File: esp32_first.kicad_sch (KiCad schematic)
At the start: 28 parts, among them J10 Conn_01x02_Socket, J11 USB_C_Receptacle_USB2.0_16P, J12 Conn_01x03_Socket, J13 Conn_01x02_Socket, J14 Conn_01x02_Socket, SW3 SW_Wuerth_450301014042, U1 ESP32-WROOM-32E, U2 MCP2561-E-SN, U3 CH340E, U4 BD33FC0FP

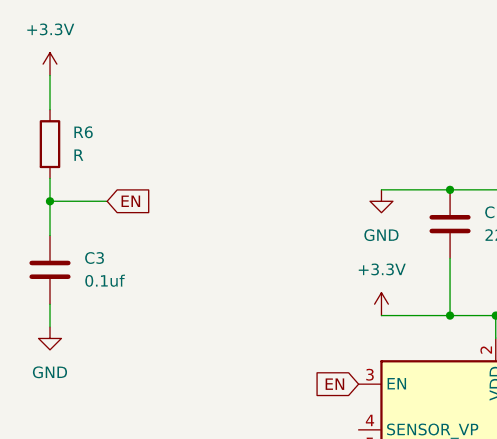
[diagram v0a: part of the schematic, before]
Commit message: STM基板から同じ部品のコピー、一部調整
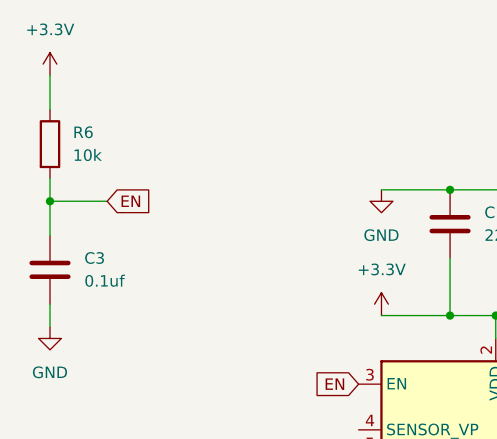
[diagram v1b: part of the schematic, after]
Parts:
- R6: value R -> 10k
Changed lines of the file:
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@@
 			)
 		)
-		(property "Value" "R"
+		(property "Value" "10k"
 			(at 31.75 27.9399 0)
 			(effects

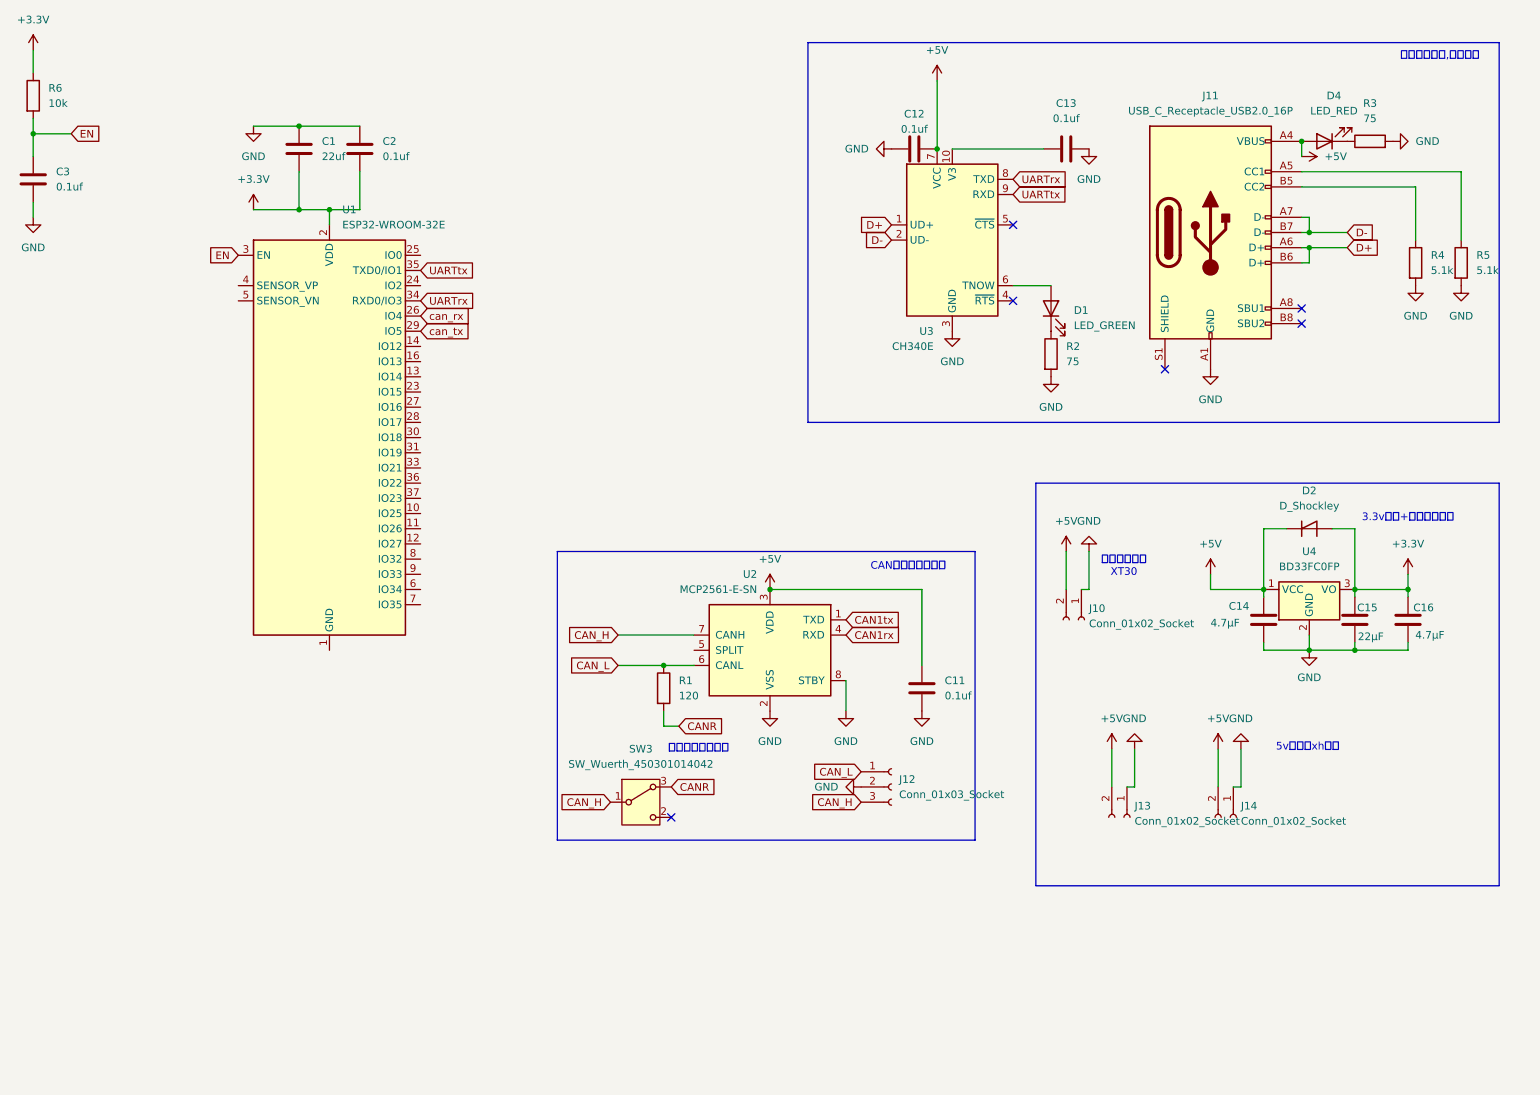
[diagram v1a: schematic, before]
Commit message: 書き込み回路の作成、不要な部品の削除
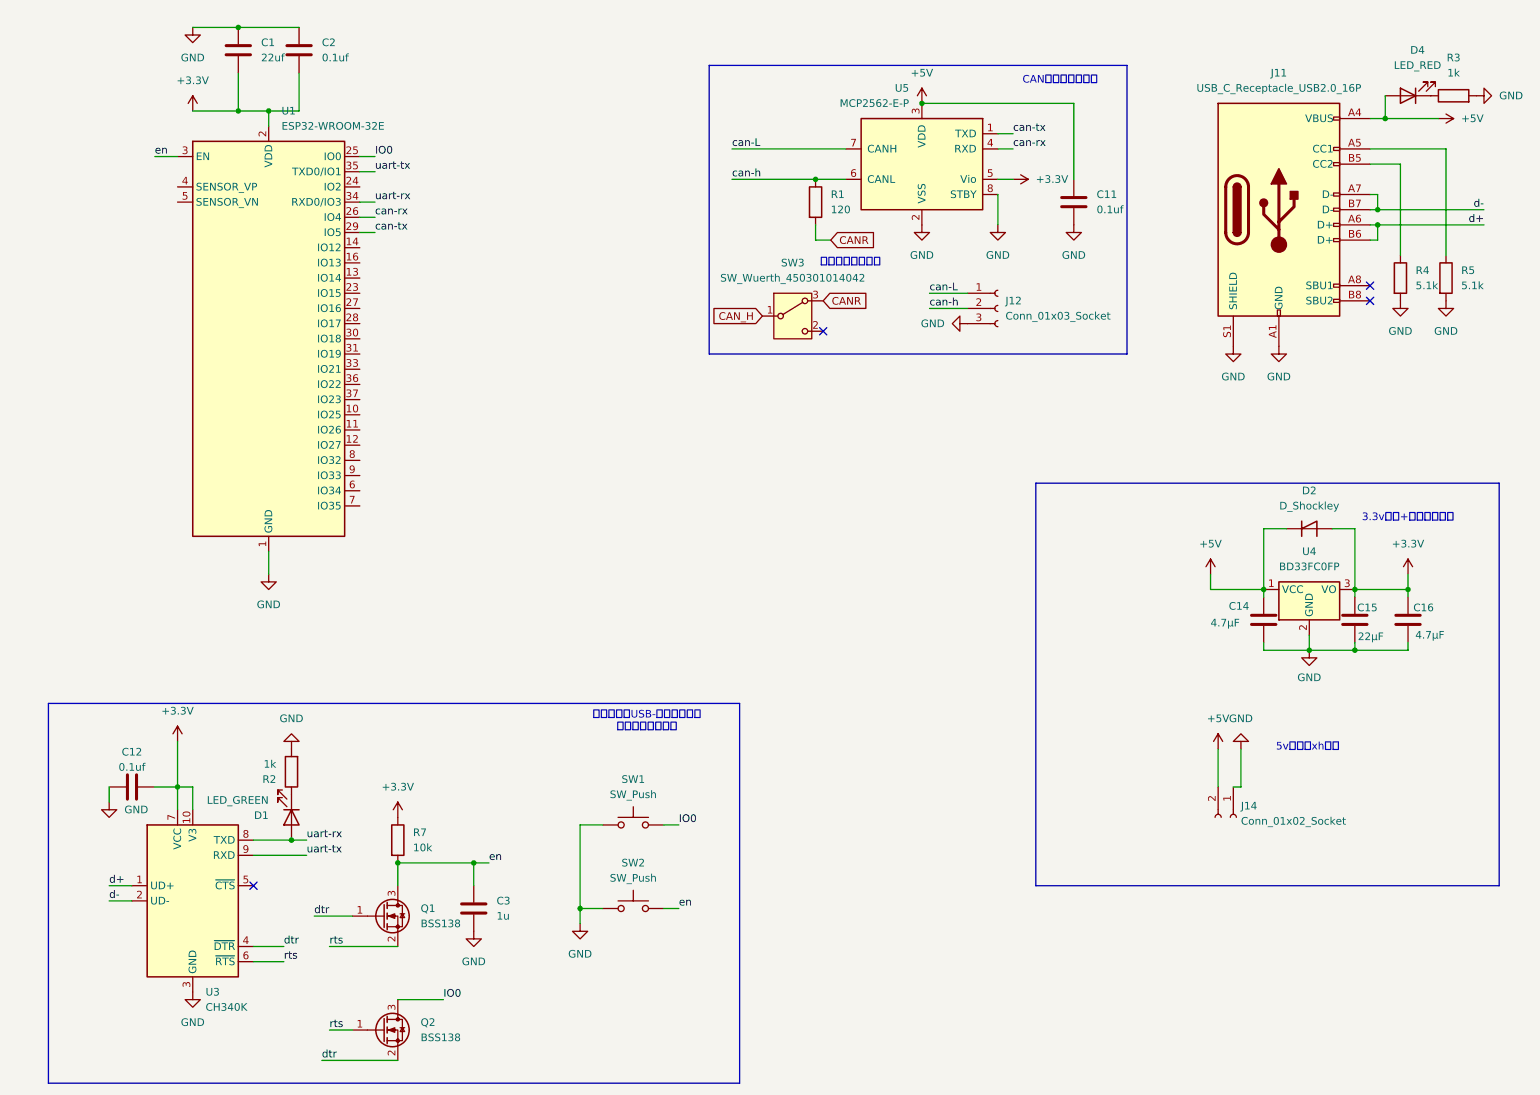
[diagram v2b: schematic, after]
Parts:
- removed C13: 0.1uf, Capacitor_SMD:C_0603_1608Metric_Pad1.08x0.95mm_HandSolder, symbol Device:C
- removed J10: Conn_01x02_Socket, Connector_AMASS:AMASS_XT30PW-F_1x02_P2.50mm_Horizontal, symbol Connector:Conn_01x02_Socket
- removed J13: Conn_01x02_Socket, Connector_JST:JST_XH_S2B-XH-A-1_1x02_P2.50mm_Horizontal, symbol Connector:Conn_01x02_Socket
- removed R6: 10k, symbol Device:R
- removed U2: MCP2561-E-SN, Package_SO:SOIC-8_3.9x4.9mm_P1.27mm, symbol Interface_CAN_LIN:MCP2561-E-SN
- removed U3: CH340E, Package_SO:MSOP-10_3x3mm_P0.5mm, symbol Interface_USB:CH340E
- added Q1, Q2: BSS138, Package_TO_SOT_SMD:SOT-23, symbol Transistor_FET:BSS138
- added R7: 10k, symbol Device:R
- added SW1, SW2: SW_Push, symbol Switch:SW_Push
- added U3: CH340K, Package_SO:SSOP-10-1EP_3.9x4.9mm_P1mm_EP2.1x3.3mm, symbol Interface_USB:CH340K
- added U5: MCP2562-E-P, Package_DIP:DIP-8_W7.62mm, symbol Interface_CAN_LIN:MCP2562-E-P
- C3: value 0.1uf -> 1u
- R2, R3: value 75 -> 1k
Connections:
- net UARTrx is gone; now on net uart-rx: U1.34 (RXD0/IO3)
- net +3.3V: now also C12.2, R7.1, U3.10 (V3), U3.7 (VCC), U5.5 (Vio)
- net +5V: now also U5.3 (VDD); no longer C12.2
- net CAN_H: no longer J12.3 (Pin_3)
- net GND: now also J11.S1 (SHIELD), J12.3 (Pin_3), U1.1 (GND), U1.15 (GND), U1.38 (GND), U1.39 (GND), SW1.1, SW2.1, U3.11 (GND), U3.3 (GND), U5.2 (VSS), U5.8 (STBY); no longer J12.2 (Pin_2)
- net IO0: now reaches U1.25 (IO0)
- net IO0: now also Q2.3 (D), SW1.2
- net uart-rx: now reaches D1.2 (A)
- net uart-rx: now also U3.8 (TXD)
- net CAN_L renamed can-L
- net can-L: now also U5.7 (CANH); no longer R1.1
- net D+ renamed d+
- net d+: now also U3.1 (UD+)
- net D- renamed d-
- net d-: now also U3.2 (UD-)
- net EN renamed en
- net en: now also Q1.3 (D), R7.2, SW2.2
- net UARTtx renamed uart-tx
- net uart-tx: now also U3.9 (RXD)
- net can_rx renamed can-rx
- net can-rx: now also U5.4 (RXD)
- net can_tx renamed can-tx
- net can-tx: now also U5.1 (TXD)
- new net can-h: J12.2 (Pin_2), R1.1, U5.6 (CANL)
- new net dtr: Q1.1 (G), Q2.2 (S), U3.4 (~{DTR})
- new net rts: Q1.2 (S), Q2.1 (G), U3.6 (~{RTS})
- no-connect marks 6 -> 4
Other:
- note added: "書き込み用USB-シリアル変換 書き込み認識回路"
- note removed: "シリアル通信,書き込み"
- note removed: "電源コネクタ XT30"
- moved on the sheet: C1, C11, C12, C2, D1, D4, J11, J12, R1, R2, R3, R4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

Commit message: フットプリントの割り当て
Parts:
- C1: footprint (none) -> Capacitor_SMD:C_0805_2012Metric_Pad1.18x1.45mm_HandSolder
- C2, C3: footprint (none) -> Capacitor_SMD:C_0603_1608Metric_Pad1.08x0.95mm_HandSolder
- R4, R5: footprint Resistor_SMD:R_1206_3216Metric_Pad1.30x1.75mm_HandSolder -> Resistor_SMD:R_0805_2012Metric_Pad1.20x1.40mm_HandSolder
- R7: footprint (none) -> Resistor_SMD:R_0805_2012Metric_Pad1.20x1.40mm_HandSolder
- SW1, SW2: footprint (none) -> Button_Switch_THT:SW_PUSH_6mm
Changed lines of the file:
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@@
 			)
 		)
-		(property "Footprint" ""
+		(property "Footprint" "Button_Switch_THT:SW_PUSH_6mm"
 			(at 129.54 143.51 0)
 			(effects
@@
 			)
 		)
-		(property "Footprint" ""
+		(property "Footprint" "Capacitor_SMD:C_0805_2012Metric_Pad1.18x1.45mm_HandSolder"
 			(at 64.4652 22.86 0)
 			(effects
@@
 			)
 		)
-		(property "Footprint" ""
+		(property "Footprint" "Capacitor_SMD:C_0603_1608Metric_Pad1.08x0.95mm_HandSolder"
 			(at 103.8352 166.37 0)
 			(effects
@@
 			)
 		)
-		(property "Footprint" "Resistor_SMD:R_1206_3216Metric_Pad1.30x1.75mm_HandSolder"
+		(property "Footprint" "Resistor_SMD:R_0805_2012Metric_Pad1.20x1.40mm_HandSolder"
 			(at 263.652 57.15 90)
 			(effects
@@
 			)
 		)
-		(property "Footprint" ""
+		(property "Footprint" "Capacitor_SMD:C_0603_1608Metric_Pad1.08x0.95mm_HandSolder"
 			(at 74.6252 22.86 0)
 			(effects
@@
 			)
 		)
-		(property "Footprint" ""
+		(property "Footprint" "Resistor_SMD:R_0805_2012Metric_Pad1.20x1.40mm_HandSolder"
 			(at 88.392 151.13 90)
 			(effects
@@
 			)
 		)
-		(property "Footprint" ""
+		(property "Footprint" "Button_Switch_THT:SW_PUSH_6mm"
 			(at 129.54 157.48 0)
 			(effects
@@
 			)
 		)
-		(property "Footprint" "Resistor_SMD:R_1206_3216Metric_Pad1.30x1.75mm_HandSolder"
+		(property "Footprint" "Resistor_SMD:R_0805_2012Metric_Pad1.20x1.40mm_HandSolder"
 			(at 256.032 57.15 90)
 			(effects

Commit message: 書き込み回路の改良
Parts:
- added C2: 0.1uf, Capacitor_SMD:C_0603_1608Metric_Pad1.08x0.95mm_HandSolder, symbol Device:C
- added J1: Conn_01x02_Socket, symbol Connector:Conn_01x02_Socket
- renumbered C12 to C1, C1 to C3, C2 to C4, C3 to C5, C11 to C6, C14 to C7, C15 to C8, C16 to C9, D4 to D3, J12 to J2, J14 to J3, J11 to J4, R2 to R1, R7 to R2, R1 to R3, R3 to R6, U3 to U1, U1 to U2, U5 to U3
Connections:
- net GND is gone; now on net +5V: C1.1, C3.1, C4.1, C5.2, C6.2, C7.2, C8.2, C9.2, J2.3 (Pin_3), J3.1 (Pin_1), J4.A1 (GND), J4.A12 (GND), J4.B1 (GND), J4.B12 (GND), J4.S1 (SHIELD), R1.2, R4.2, R5.2, R6.2, SW1.1, SW2.1, U1.11 (GND), U1.3 (GND), U2.1 (GND), U2.15 (GND), U2.38 (GND), U2.39 (GND), U3.2 (VSS), U3.8 (STBY), U4.2 (GND)
- net +3.3V: no longer C1.2, U1.10 (V3), U1.7 (VCC)
- net +5V: now also C1.2, U1.7 (VCC), C2.1
- net uart-rx: now also J1.2 (Pin_2)
- net uart-tx: now also J1.1 (Pin_1)
- new net: C2.2, U1.10 (V3)
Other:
- moved on the sheet: C1
